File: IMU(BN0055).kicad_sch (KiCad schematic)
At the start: 7 parts, among them U1 BNO055

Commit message: Whole Circuit Integration
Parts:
- C5, C6, C7, C8: footprint Capacitor_SMD:CP_Elec_4x3 -> Capacitor_SMD:C_1206_3216Metric
- Optional2, Pull-Up2: footprint Resistor_SMD:R_0603_1608Metric_Pad0.98x0.95mm_HandSolder -> Resistor_SMD:R_1206_3216Metric
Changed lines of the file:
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@@
 			)
 		)
-		(property "Footprint" "Capacitor_SMD:CP_Elec_4x3"
+		(property "Footprint" "Capacitor_SMD:C_1206_3216Metric"
 			(at 194.31 94.2848 0)
 			(effects
@@
 			)
 		)
-		(property "Footprint" "Capacitor_SMD:CP_Elec_4x3"
+		(property "Footprint" "Capacitor_SMD:C_1206_3216Metric"
 			(at 134.62 93.6752 0)
 			(effects
@@
 			)
 		)
-		(property "Footprint" "Capacitor_SMD:CP_Elec_4x3"
+		(property "Footprint" "Capacitor_SMD:C_1206_3216Metric"
 			(at 162.2552 63.5 0)
 			(effects
@@
 			)
 		)
-		(property "Footprint" "Resistor_SMD:R_0603_1608Metric_Pad0.98x0.95mm_HandSolder"
+		(property "Footprint" "Resistor_SMD:R_1206_3216Metric"
 			(at 113.792 58.42 90)
 			(effects
@@
 			)
 		)
-		(property "Footprint" "Resistor_SMD:R_0603_1608Metric_Pad0.98x0.95mm_HandSolder"
+		(property "Footprint" "Resistor_SMD:R_1206_3216Metric"
 			(at 126.492 64.77 90)
 			(effects
@@
 			)
 		)
-		(property "Footprint" "Capacitor_SMD:CP_Elec_4x3"
+		(property "Footprint" "Capacitor_SMD:C_1206_3216Metric"
 			(at 174.9552 63.5 0)
 			(effects

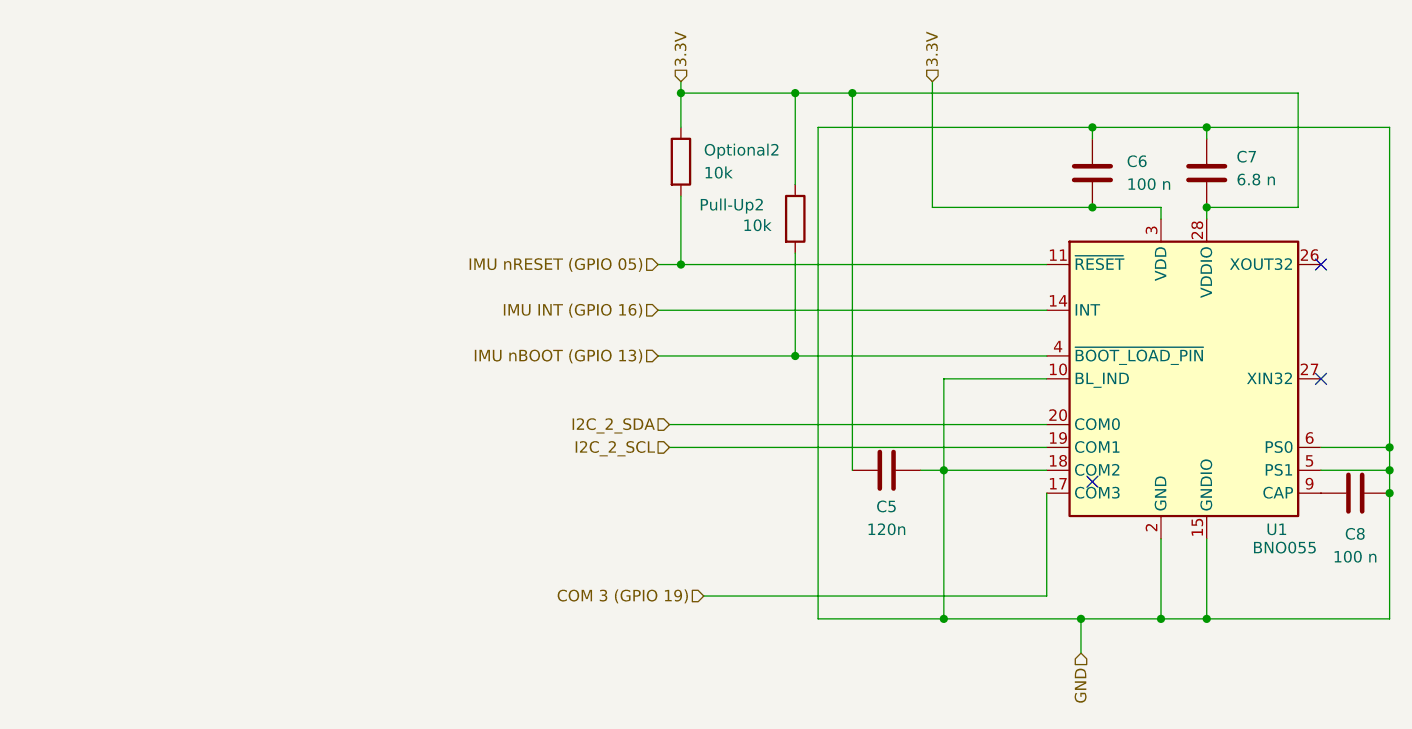
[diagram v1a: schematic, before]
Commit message: Reorganized schematic and resolved ERC errors
Resolved some of the ERC errors related to disconnected pins and power flags. Renamed GPIO pins on 40-pin header. Changed ADC power supply to 3.3V and schmitt trigger circuit power supply to 5V. Connected 5V, 3.3V, and GND pins of 40-pin header. Assigned footprint for 40-pin header based on dimensions of expansion header on Jetson Nano Carrier Board.

Also moved IMU and 40-pin header KiCAD project files into their own folders.
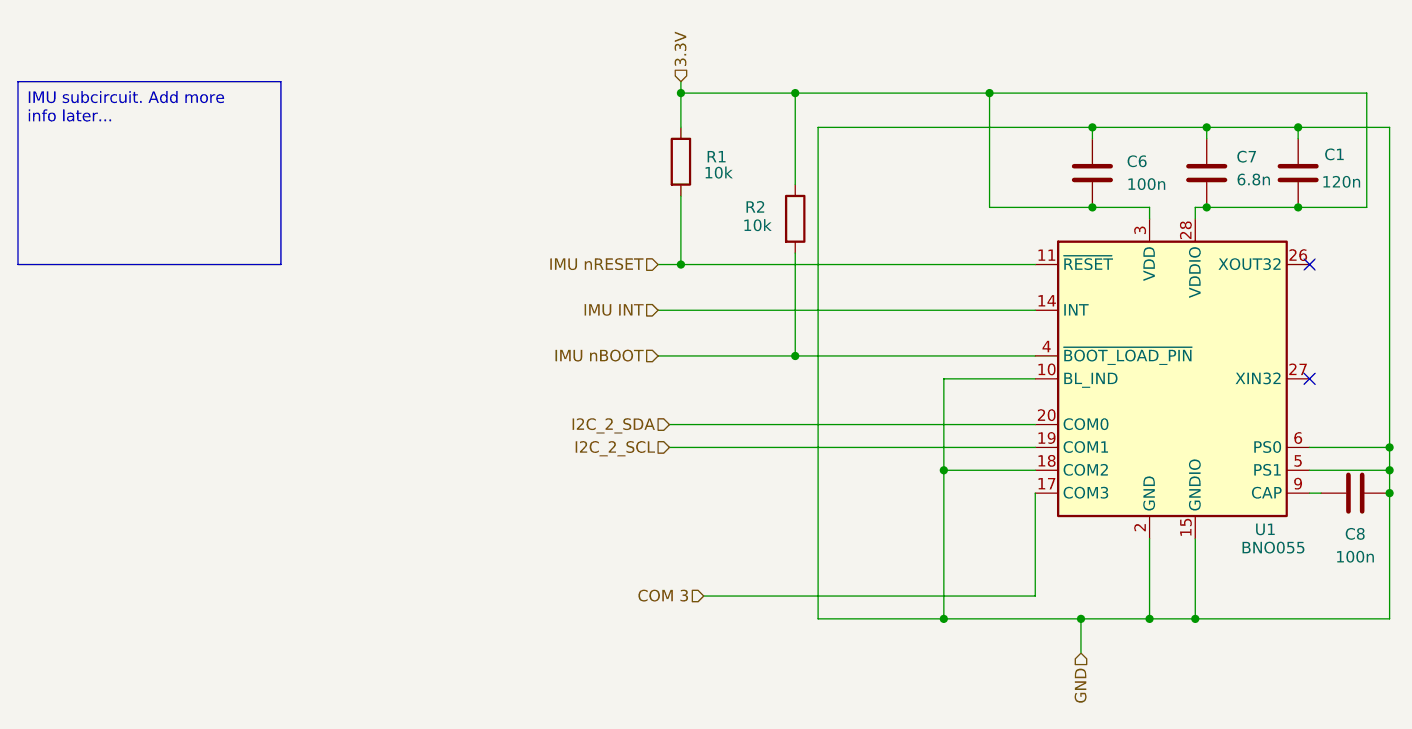
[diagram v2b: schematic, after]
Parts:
- removed C5: 120n, Capacitor_SMD:C_1206_3216Metric, symbol Device:C
- added C1: 120n, Capacitor_SMD:C_1206_3216Metric, symbol Device:C
- C6, C8: value 100 n -> 100n
- C7: value 6.8 n -> 6.8n
- renumbered Optional2 to R1, Pull-Up2 to R2
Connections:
- net 3.3V: now also C1.2
- net GND: now also C1.1
- net COM 3 (GPIO 19) renamed COM 3
- net IMU INT (GPIO 16) renamed IMU INT
- net IMU nBOOT (GPIO 13) renamed IMU nBOOT
- net IMU nRESET (GPIO 05) renamed IMU nRESET
- no-connect marks 3 -> 2

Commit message: Started PCB Layout
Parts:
- renumbered C6 to C1, C7 to C2, C1 to C3, C8 to C4
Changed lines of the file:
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@@
 		(on_board yes)
 		(dnp no)
-		(property "Reference" "C8"
+		(property "Reference" "C4"
 			(at 190.5 99.822 90)
 			(effects
@@
 			(project "WholeCircuitIntegration(Flagged)"
 				(path "/fac81d63-8655-47f4-bf8e-62708c29b8c6/330580df-b1d0-4440-aa2e-172d63d89a0a"
-					(reference "C8")
+					(reference "C4")
 					(unit 1)
 				)
@@
 		(dnp no)
 		(fields_autoplaced yes)
-		(property "Reference" "C6"
+		(property "Reference" "C1"
 			(at 165.1 58.4199 0)
 			(effects
@@
 			(project "WholeCircuitIntegration(Flagged)"
 				(path "/fac81d63-8655-47f4-bf8e-62708c29b8c6/330580df-b1d0-4440-aa2e-172d63d89a0a"
-					(reference "C6")
+					(reference "C1")
 					(unit 1)
 				)
@@
 		(on_board yes)
 		(dnp no)
-		(property "Reference" "C7"
+		(property "Reference" "C2"
 			(at 177.292 57.912 0)
 			(effects
@@
 			(project "WholeCircuitIntegration(Flagged)"
 				(path "/fac81d63-8655-47f4-bf8e-62708c29b8c6/330580df-b1d0-4440-aa2e-172d63d89a0a"
-					(reference "C7")
+					(reference "C2")
 					(unit 1)
 				)
@@
 		(on_board yes)
 		(dnp no)
-		(property "Reference" "C1"
+		(property "Reference" "C3"
 			(at 188.214 57.658 0)
 			(effects
@@
 			(project "WholeCircuitIntegration(Flagged)"
 				(path "/fac81d63-8655-47f4-bf8e-62708c29b8c6/330580df-b1d0-4440-aa2e-172d63d89a0a"
-					(reference "C1")
-					(unit 1)
-				)
+					(reference "C3")
+					(unit 1)
+				)
